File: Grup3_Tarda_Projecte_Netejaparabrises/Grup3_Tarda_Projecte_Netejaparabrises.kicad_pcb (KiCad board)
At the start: 4 copper layers, 162.4 x 126.5 mm, 89 parts, among them IC1 L78S05CV, IC2 PIC18F258-I_SO, J1 Screw_Terminal_01x02, J10 Screw_Terminal_01x02, J11 Screw_Terminal_01x02, J12 Screw_Terminal_01x02, J2 BOTONERA, J3 PROGRAMMING CON, J4 JP1, J5 DE9_Plug_MountingHoles, J6 DE9_Plug_MountingHoles, J7 CONEXIOSENSOR, J8 Screw_Terminal_01x02, J9 Screw_Terminal_01x02, K1 1393280-6, K2 1393280-6, K3 1393280-6, K4 1393280-6, K5 1393280-6, K6 1393280-6, K7 1393280-6, K8 1393280-6, K9 1393280-6, Q1 BC817-25_RF, Q2 BC817-25_RF, Q3 BC817-25_RF, Q4 BC817-25_RF, Q5 BC817-25_RF, Q6 BC817-25_RF, Q7 BC817-25_RF, U1 Value, U2 LM393, Y1 ABLS2-8.000MHZ-D4Y-T

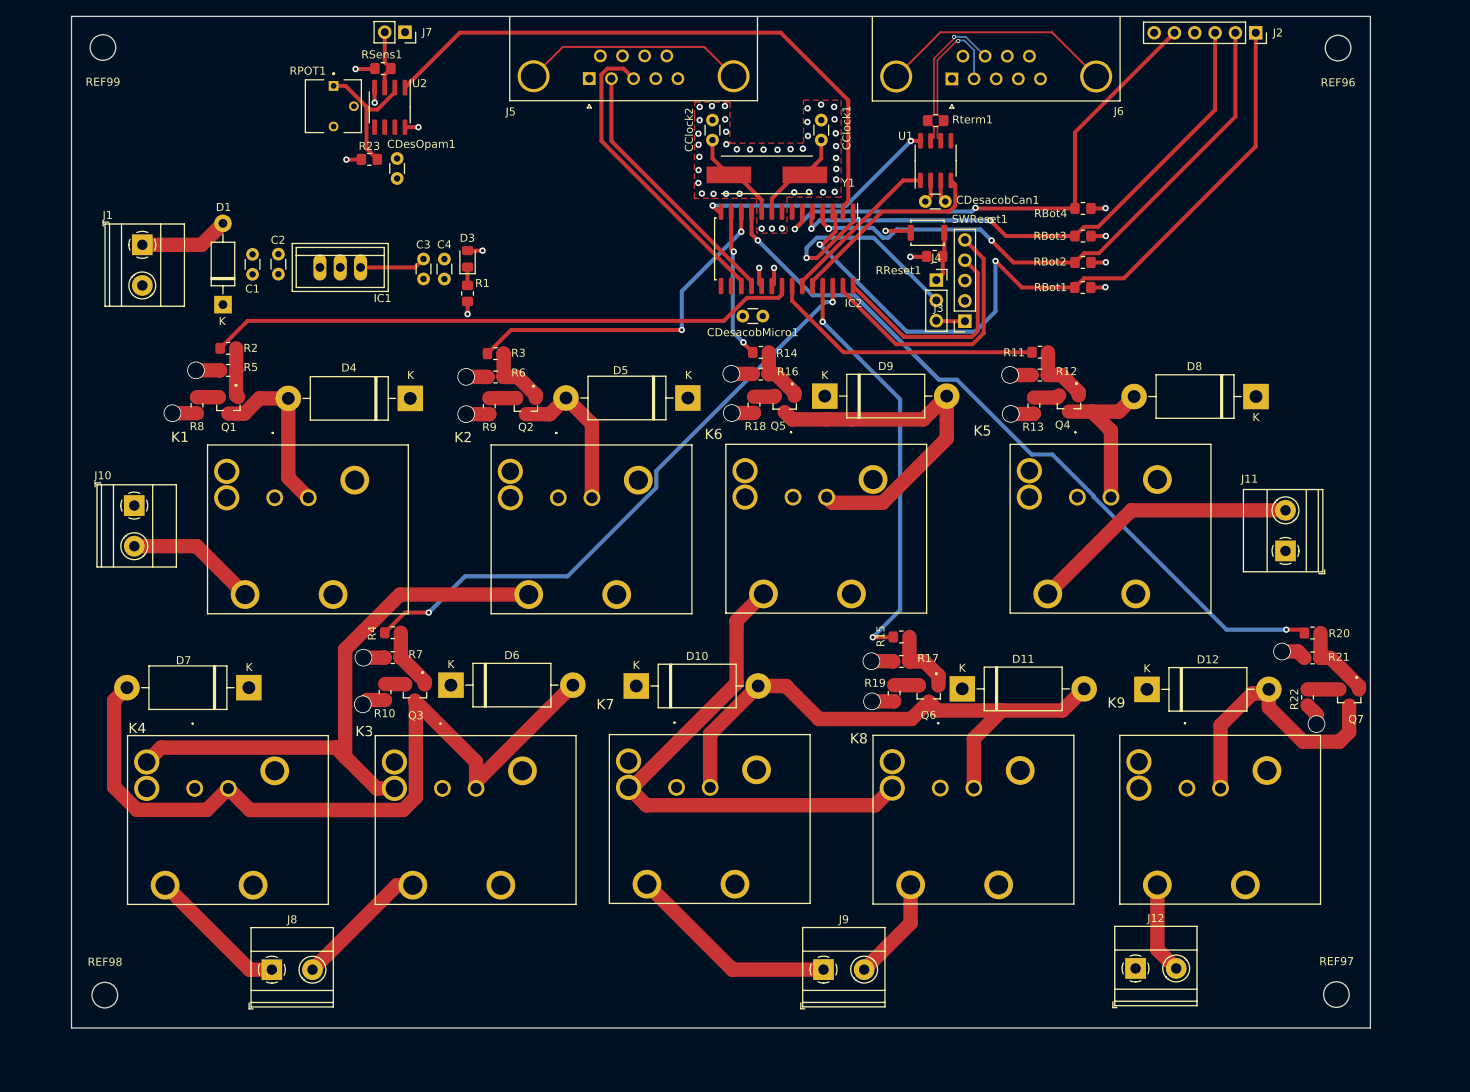
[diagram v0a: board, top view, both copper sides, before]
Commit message: placing rooting
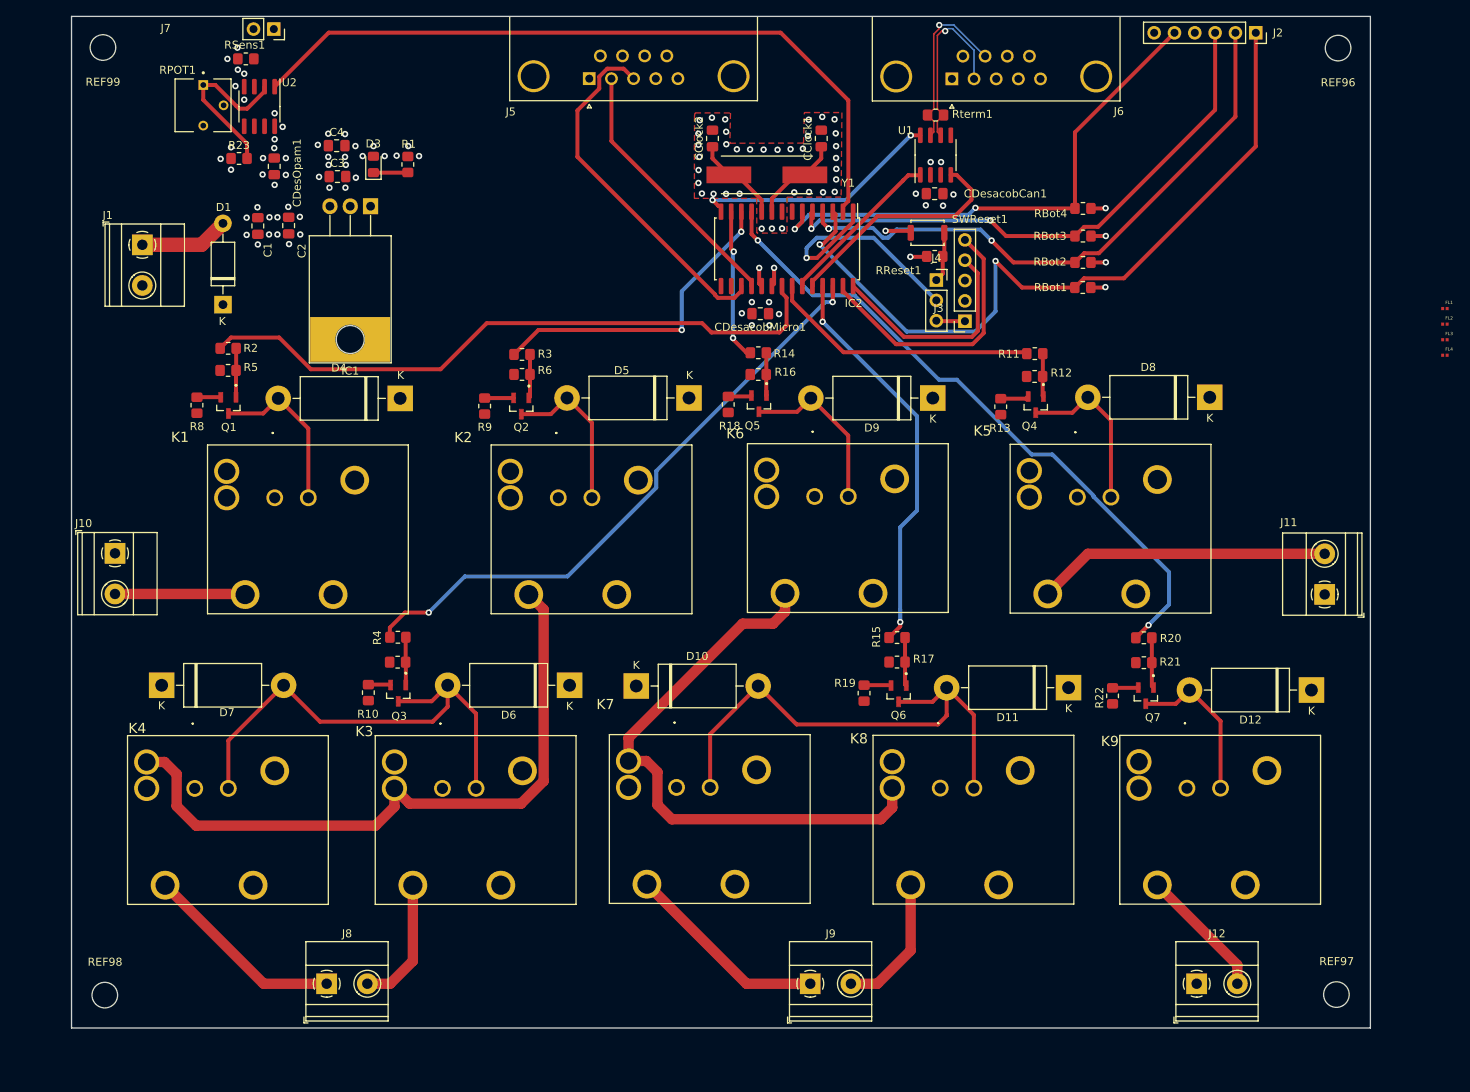
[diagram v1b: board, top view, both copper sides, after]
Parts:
- added FL1: BLM03HD331SZ1D, BLM03HD331SZ1D:BEADC0603X33N, F.Cu at (231.8, 63.3)
- added FL2: BLM03HD331SZ1D, BLM03HD331SZ1D:BEADC0603X33N, F.Cu at (231.8, 65.3)
- added FL3: BLM03HD331SZ1D, BLM03HD331SZ1D:BEADC0603X33N, F.Cu at (231.8, 67.2)
- added FL4: BLM03HD331SZ1D, BLM03HD331SZ1D:BEADC0603X33N, F.Cu at (231.8, 69.2)
- C1, C2, C3, C4, CClock1, CClock2, CDesOpam1, CDesacobCan1, CDesacobMicro1: footprint Capacitor_THT:C_Disc_D3.0mm_W1.6mm_P2.50mm -> Capacitor_SMD:C_0805_2012Metric_Pad1.18x1.45mm_HandSolder
- IC1: footprint L78S05CV:TO-220-STANDING -> Libreia:TO-220-3_Horizontal_TabDown_mod
- moved Q7 25.4 mm to (194.4, 111.7)
- moved R22 24.4 mm to (190.3, 111.7)
- moved R20 21.1 mm to (194.2, 104.5)
- moved R21 21.1 mm to (194.2, 107.6)
- moved D12 20.6 mm to (215.2, 111.0), turned to 180 degrees
- moved C4 19.6 mm to (93.3, 43.0), turned to 0 degrees
- moved R1 17.8 mm to (102.2, 45.3), turned to 90 degrees
- moved RSens1 17.2 mm to (82.0, 32.1)
- moved D3 16.7 mm to (97.9, 45.3)
- moved J7 16.4 mm to (85.5, 28.4)
- moved R23 16.3 mm to (81.1, 44.5)
- moved RPOT1 16.3 mm to (76.6, 37.9)
- moved U2 16.3 mm to (83.7, 38.0)
- moved CDesOpam1 15.4 mm to (85.5, 45.5)
- moved C3 14.9 mm to (93.4, 46.8), turned to 0 degrees
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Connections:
- K7 pad 3: GNDPWR -> EN2
- K7 pad 5: EN2 -> GNDPWR
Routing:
- net GNDPWR: track 39.9 -> 0.00 mm, vias 14 -> 0
- net /Potencia/Vc_m1: track 99.0 -> 63.0 mm
- net unconnected-(J6-PAD-Pad0): track 29.6 -> 0.00 mm
- net unconnected-(J5-PAD-Pad0): track 28.0 -> 0.00 mm
- net /Potencia/Vc_EN2: track 45.8 -> 21.4 mm
- net +VCC: track 28.5 -> 11.9 mm, vias 9 -> 6
- net Sensordig_o: track 76.0 -> 92.2 mm
- net /Potencia/Vc_lu: track 33.6 -> 20.0 mm
- net EN1: track 73.0 -> 84.6 mm
- net DriverLuneta: track 92.6 -> 82.5 mm
- net GND: track 14.5 -> 5.65 mm, vias 45 -> 38
- net VMOT1-: track 17.7 -> 25.3 mm
- net /Analog/Vsensor: track 7.57 -> 0.00 mm
- net DriverB1: track 74.1 -> 81.4 mm
- net /Digital/Tx: track 38.5 -> 45.2 mm
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
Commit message: redefinicio copper pours, rerouting, final de carrera i teardrops
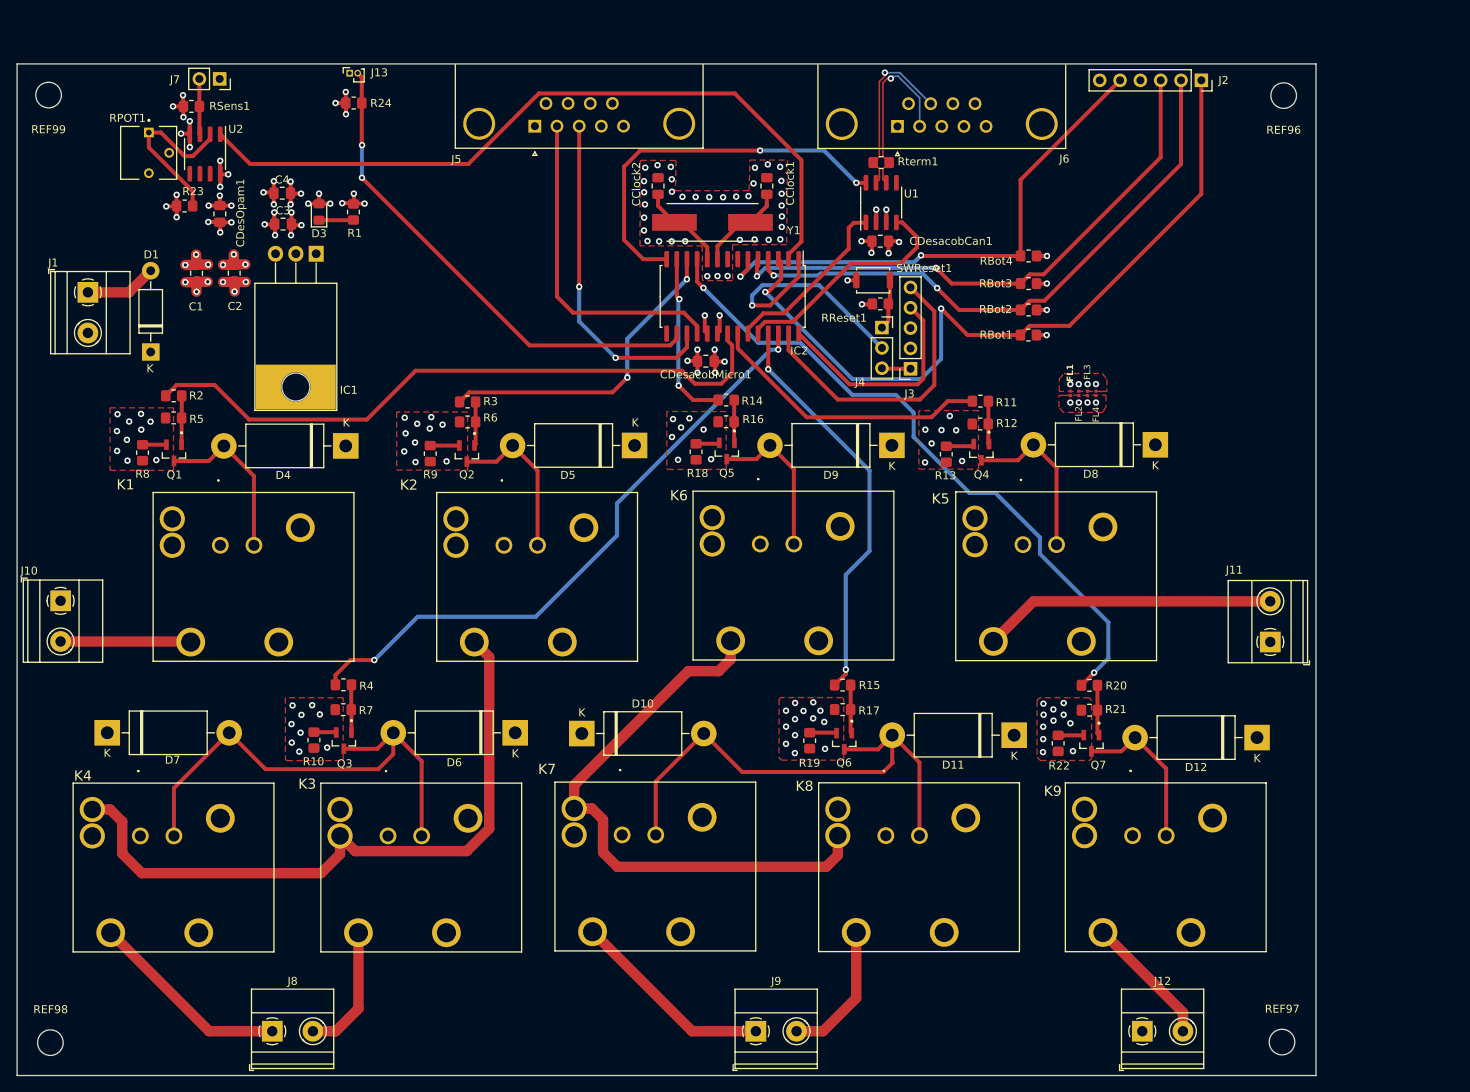
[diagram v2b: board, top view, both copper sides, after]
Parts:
- added J13: FINAL DE CARRERA, Connector_PinSocket_1.00mm:PinSocket_1x02_P1.00mm_Vertical, F.Cu at (94.9, 33.9)
- added R24: 22k, Resistor_SMD:R_0805_2012Metric_Pad1.20x1.40mm_HandSolder, F.Cu at (95.4, 37.6)
- moved FL1 48.0 mm to (185.0, 73.9), turned to 90 degrees
- moved FL2 46.6 mm to (186.1, 73.9), turned to 90 degrees
- moved FL3 45.2 mm to (187.2, 73.9), turned to 90 degrees
- moved FL4 43.9 mm to (188.2, 73.9), turned to 90 degrees
- moved D1 10.8 mm to (70.1, 68.7)
- moved C1 9.67 mm to (75.8, 58.9)
- moved J7 9.20 mm to (78.7, 34.6)
- moved Q4 9.03 mm to (173.9, 81.3)
- moved CClock2 9.03 mm to (133.5, 48.0)
- moved D3 9.03 mm to (91.1, 51.2)
- moved U2 9.03 mm to (76.8, 44.0)
- moved J2 9.03 mm to (201.4, 34.8)
- moved CDesacobCan1 9.03 mm to (161.2, 54.9)
- moved CDesacobMicro1 9.03 mm to (139.4, 69.9)
- moved D10 9.03 mm to (124.0, 116.4)
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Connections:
- IC2 pad 16: unconnected-(IC2-RC5/SDO-Pad16) -> /Digital/Vfinal
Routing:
- net /Digital/Vfinal: track 0.00 -> 62.4 mm, vias 0 -> 2
- net +VCC: track 11.9 -> 46.7 mm, vias 6 -> 33
- net GND: track 5.65 -> 37.3 mm, vias 38 -> 66
- net STB: track 30.7 -> 48.2 mm
- net VBAT: track 0.00 -> 8.33 mm, vias 0 -> 6
- net GNDPWR: track 0.00 -> 8.32 mm, vias 0 -> 77
- net /Digital/Rx: track 33.2 -> 41.3 mm
- net /Analog/Vsensor: track 0.00 -> 6.94 mm
- net /Digital/Tx: track 45.2 -> 42.0 mm, vias 0 -> 2
- net PGC: track 34.2 -> 37.0 mm
- net EnableM2: track 19.0 -> 21.7 mm
- net /Alimentacio/Vbat: track 11.2 -> 8.97 mm
- net Sensordig_o: track 92.2 -> 94.3 mm
- net /Potencia/Vc_EN2: track 21.4 -> 19.7 mm
- net DriverB2: track 33.9 -> 35.6 mm
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- added copper zone on F.Cu, net GNDPWR

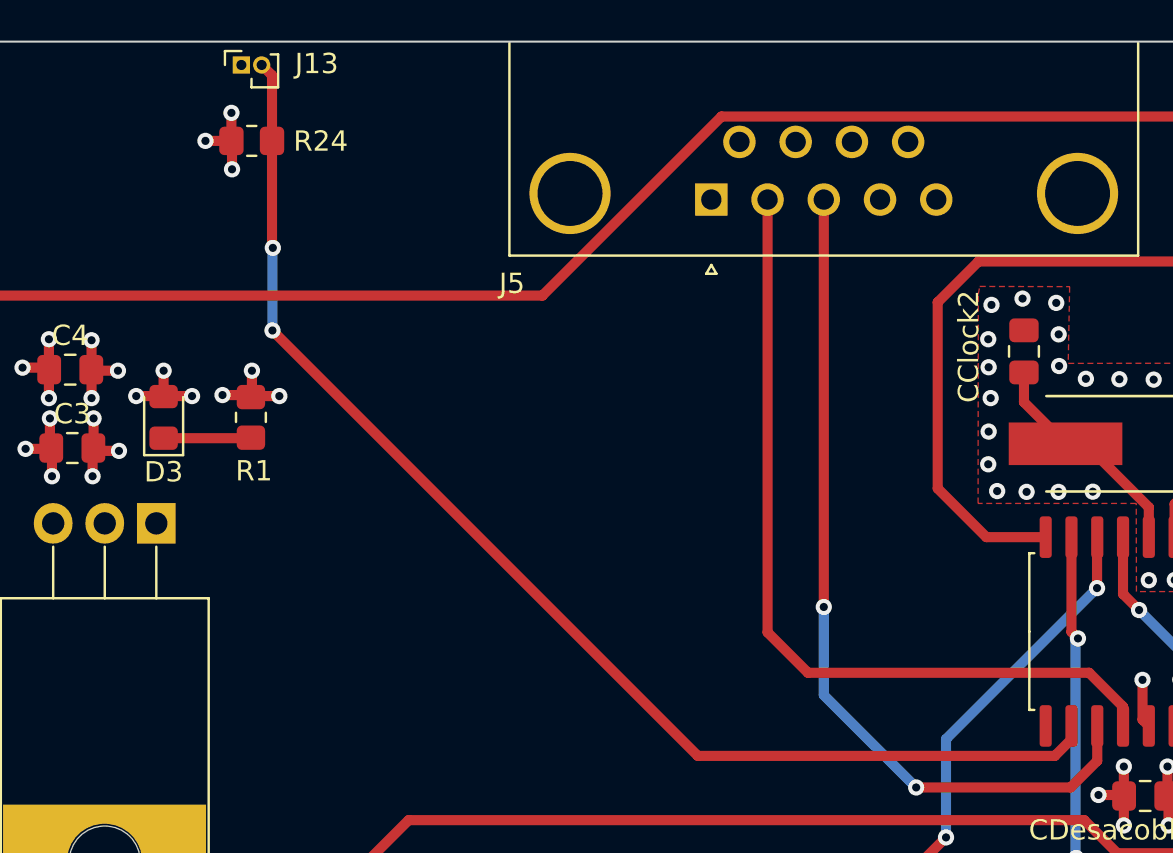
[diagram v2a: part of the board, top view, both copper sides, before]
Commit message: afegits els finals de carrera dels motors
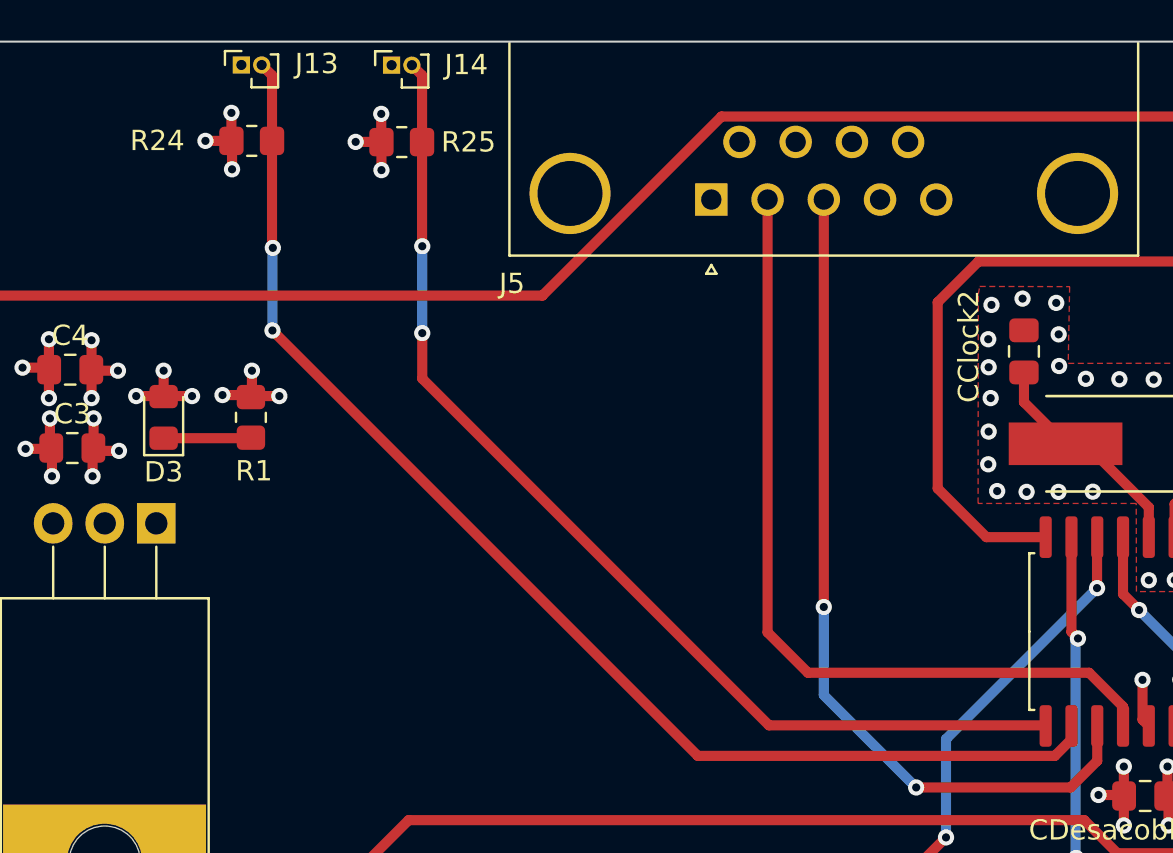
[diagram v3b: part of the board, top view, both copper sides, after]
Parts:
- added J14: FINAL DE CARRERA, Connector_PinSocket_1.00mm:PinSocket_1x02_P1.00mm_Vertical, F.Cu at (102.3, 33.9)
- added R25: 22k, Resistor_SMD:R_0805_2012Metric_Pad1.20x1.40mm_HandSolder, F.Cu at (102.8, 37.7)
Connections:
- net /Digital/Vfinal renamed /Digital/Vfin_front
- IC2 pad 15: unconnected-(IC2-RC4/SDI/SDA-Pad15) -> /Digital/Vfin_back
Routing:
- net /Digital/Vfin_back: track 0.00 -> 53.4 mm, vias 0 -> 2
- net +VCC: track 46.7 -> 50.7 mm, vias 33 -> 36
